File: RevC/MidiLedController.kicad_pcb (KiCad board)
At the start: 2 copper layers, 99.8 x 100.1 mm, 151 parts, among them J1 Molex 2Way KK254, J12 Barrel_Jack, Q1 MBT3946DW1T1, Q10 MBT3946DW1T1, Q11 MBT3946DW1T1, Q12 MBT3946DW1T1, Q13 MBT3946DW1T1, Q14 MBT3946DW1T1, Q15 MBT3946DW1T1, Q16 MBT3946DW1T1, Q17 MBT3946DW1T1, Q18 MBT3946DW1T1, Q2 MBT3946DW1T1, Q21 DMG2301L, Q3 MBT3946DW1T1, Q4 MBT3946DW1T1, Q5 MBT3946DW1T1, Q6 MBT3946DW1T1, Q7 MBT3946DW1T1, Q8 MBT3946DW1T1, Q9 MBT3946DW1T1, SW1 SW_DIP_x04, SW2 SW_SPST, U1 RAx4_4 1K, U10 RAx4_4 1K, U11 RAx4_4 1K, U12 RAx4_4 1K, U13 RAx4_4 1K, U14 RAx4_4 1K, U15 RAx4_4 1K, U16 RAx4_4 1K, U17 RAx4_4 1K, U18 RAx4_4 1K, U2 RAx4_4 1K, U20 STM32F051K8Tx, U21 6N135S, U22 TPS54202, U23 L7805, U24 MCP1754ST-3302E/CB, U25 NCP51460SN33T1G, U3 RAx4_4 1K, U4 RAx4_4 1K, U5 RAx4_4 1K, U6 RAx4_4 1K, U7 RAx4_4 1K, U8 RAx4_4 1K, U9 RAx4_4 1K

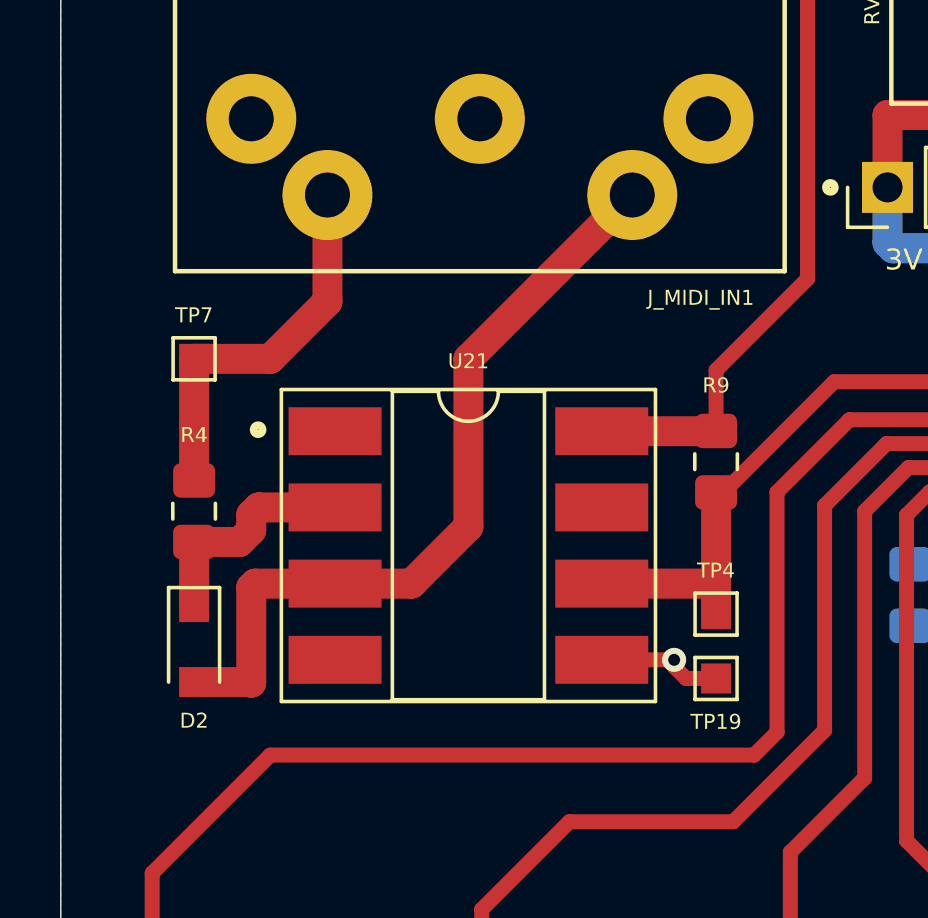
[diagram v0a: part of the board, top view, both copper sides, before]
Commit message: Replaced 6N135 SMDIP8 with H11L1 SMDIP6
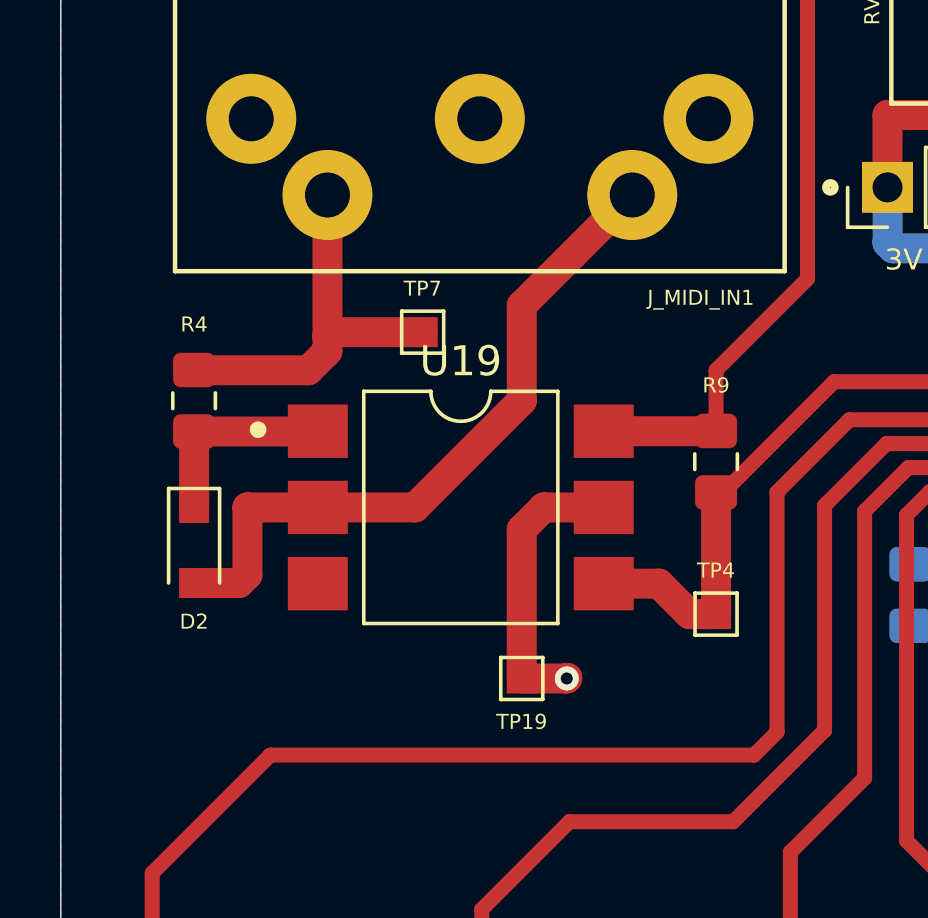
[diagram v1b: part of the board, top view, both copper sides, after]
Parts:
- removed U21: 6N135S, Package_DIP:DIP-8_W8.89mm_SMDSocket_LongPads
- added U19: H11L1, Package_DIP:SMDIP-6_W9.53mm, F.Cu at (106.7, 69.1)
- C29, C31: value 1u MLCC 10V X7R -> 1u
- L2: value 6.8uH -> 4.7uH
- Q21: value DMG2301L -> HX2301A
- U22: value TPS54202 -> TPS54202DDCR
- moved TP7 7.67 mm to (105.4, 63.2)
- moved TP19 6.48 mm to (108.7, 74.8)
- moved R4 3.68 mm to (97.8, 65.5)
- moved D2 3.30 mm to (97.8, 70.4)
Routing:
- net GNDS: track 116.7 -> 122.0 mm
- net Net-(D2-Pad2): track 26.5 -> 23.1 mm
- net Net-(D2-Pad1): track 7.65 -> 6.68 mm

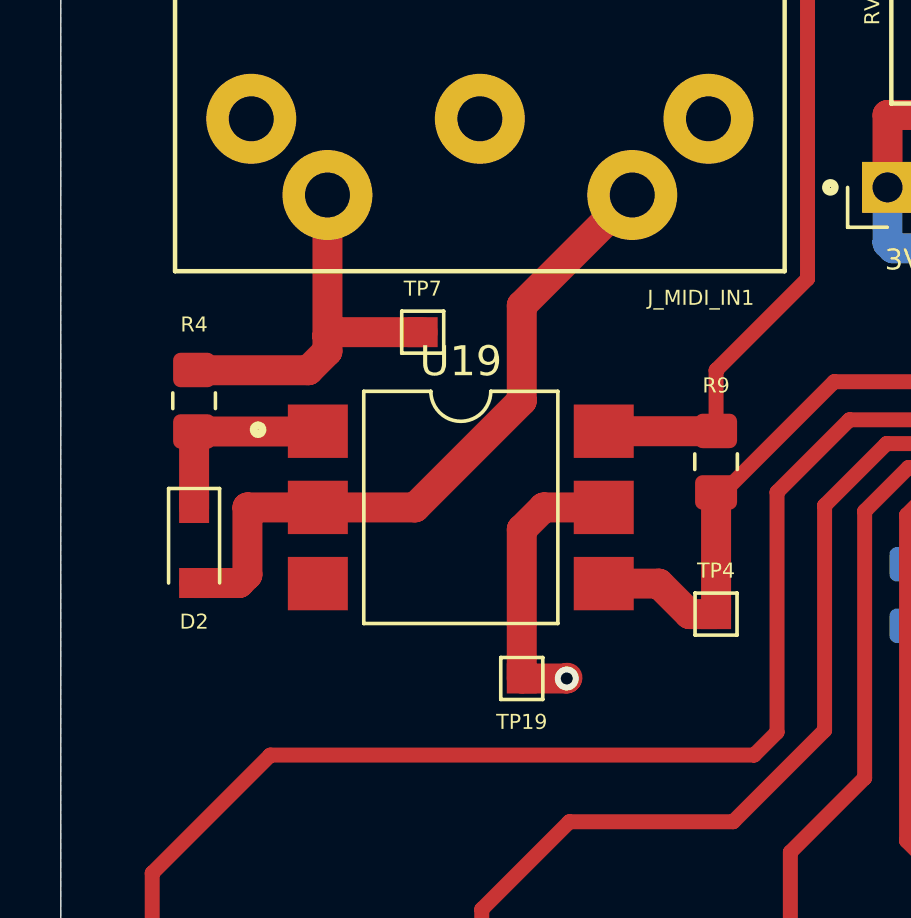
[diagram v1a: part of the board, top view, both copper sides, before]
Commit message: Replaced H11L1 SMD6 with TLP2361 SO5
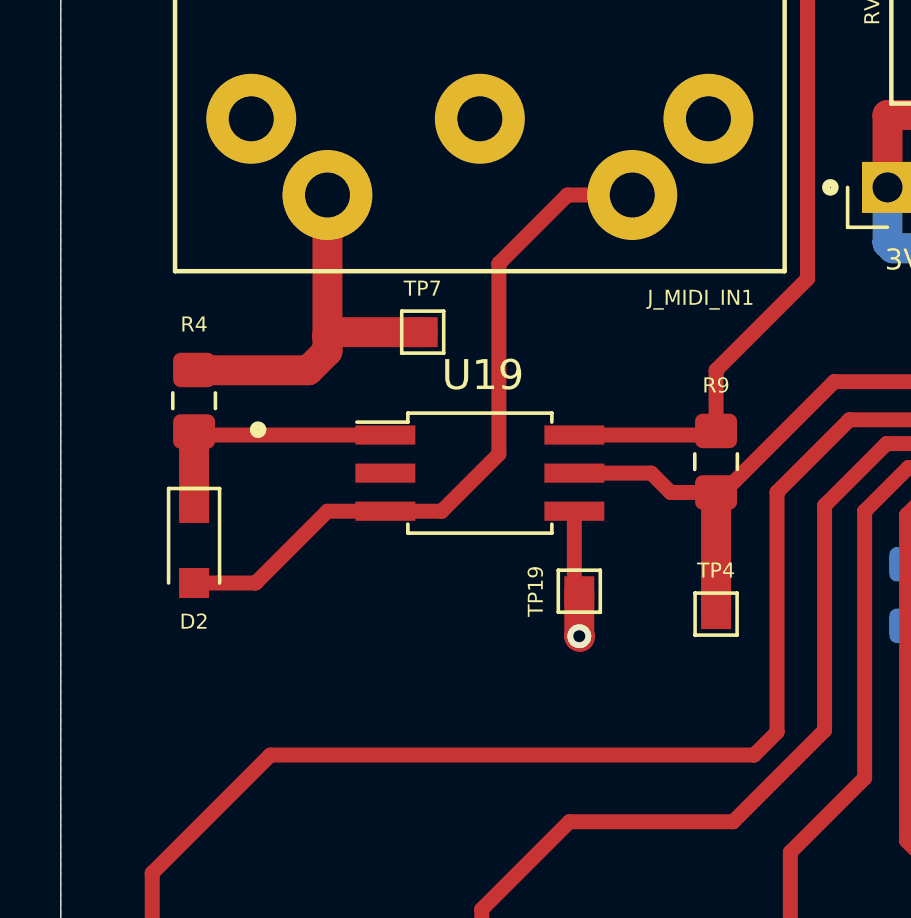
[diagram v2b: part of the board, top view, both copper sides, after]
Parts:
- U19: value H11L1 -> TLP2361; footprint Package_DIP:SMDIP-6_W9.53mm -> Package_SO:SO-6_4.4x3.6mm_P1.27mm
- moved TP19 3.48 mm to (110.6, 71.9), turned to 90 degrees
- moved U19 1.31 mm to (107.3, 67.9)
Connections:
- U19 pad 2: Net-(D2-Pad2) -> (no net)
- U19 pad 3: Net-(U19-Pad3) -> Net-(D2-Pad2)
- U19 pad 4: /MIDI_RX -> GNDS
- U19 pad 5: GNDS -> /MIDI_RX
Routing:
- net GNDS: track 122.0 -> 116.7 mm
- net Net-(D2-Pad1): track 6.68 -> 8.97 mm
- net +5V: track 588.9 -> 590.0 mm
- net /MIDI_RX: track 25.6 -> 26.4 mm
- net Net-(D2-Pad2): track 23.1 -> 23.7 mm

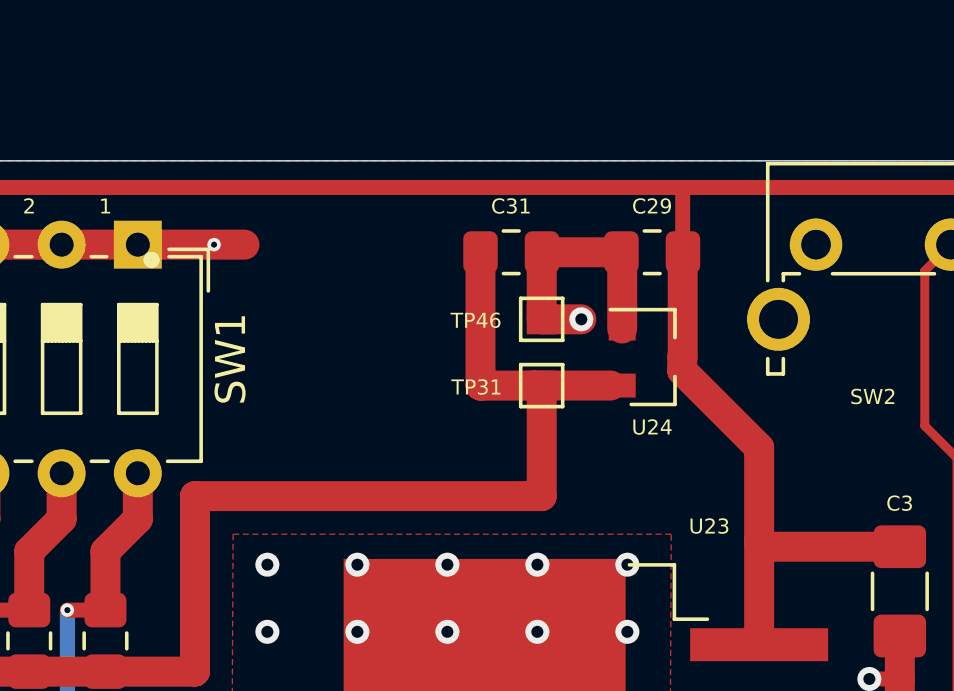
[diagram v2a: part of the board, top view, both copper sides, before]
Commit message: hw update
switched MCP1754 (SOT23-3) to LP3992 (SOT23-5)
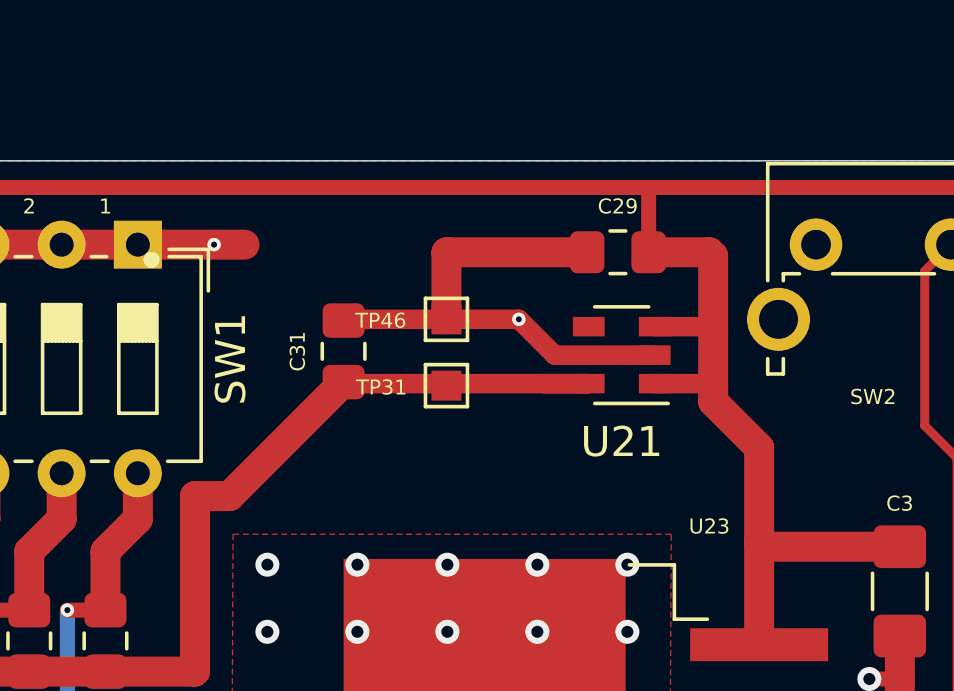
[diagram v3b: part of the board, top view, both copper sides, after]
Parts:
- removed U24: MCP1754ST-3302E/CB, Package_TO_SOT_SMD:SOT-23
- added U21: LP3993-33B5F, Package_TO_SOT_SMD:SOT-23-5, F.Cu at (163.4, 49.9)
- moved C31 6.49 mm to (154.2, 49.8), turned to 90 degrees
- moved TP31 3.18 mm to (157.6, 50.9)
- moved TP46 3.18 mm to (157.6, 48.7)
- moved C29 1.14 mm to (163.3, 46.5)
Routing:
- net GNDS: track 116.7 -> 125.8 mm
- net +3V3: track 110.7 -> 102.9 mm
- net +5V: track 590.0 -> 596.3 mm
